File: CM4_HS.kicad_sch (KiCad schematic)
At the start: 7 parts, among them J14 CM4/5 Module B, SW3 SW_Slide_DPDT

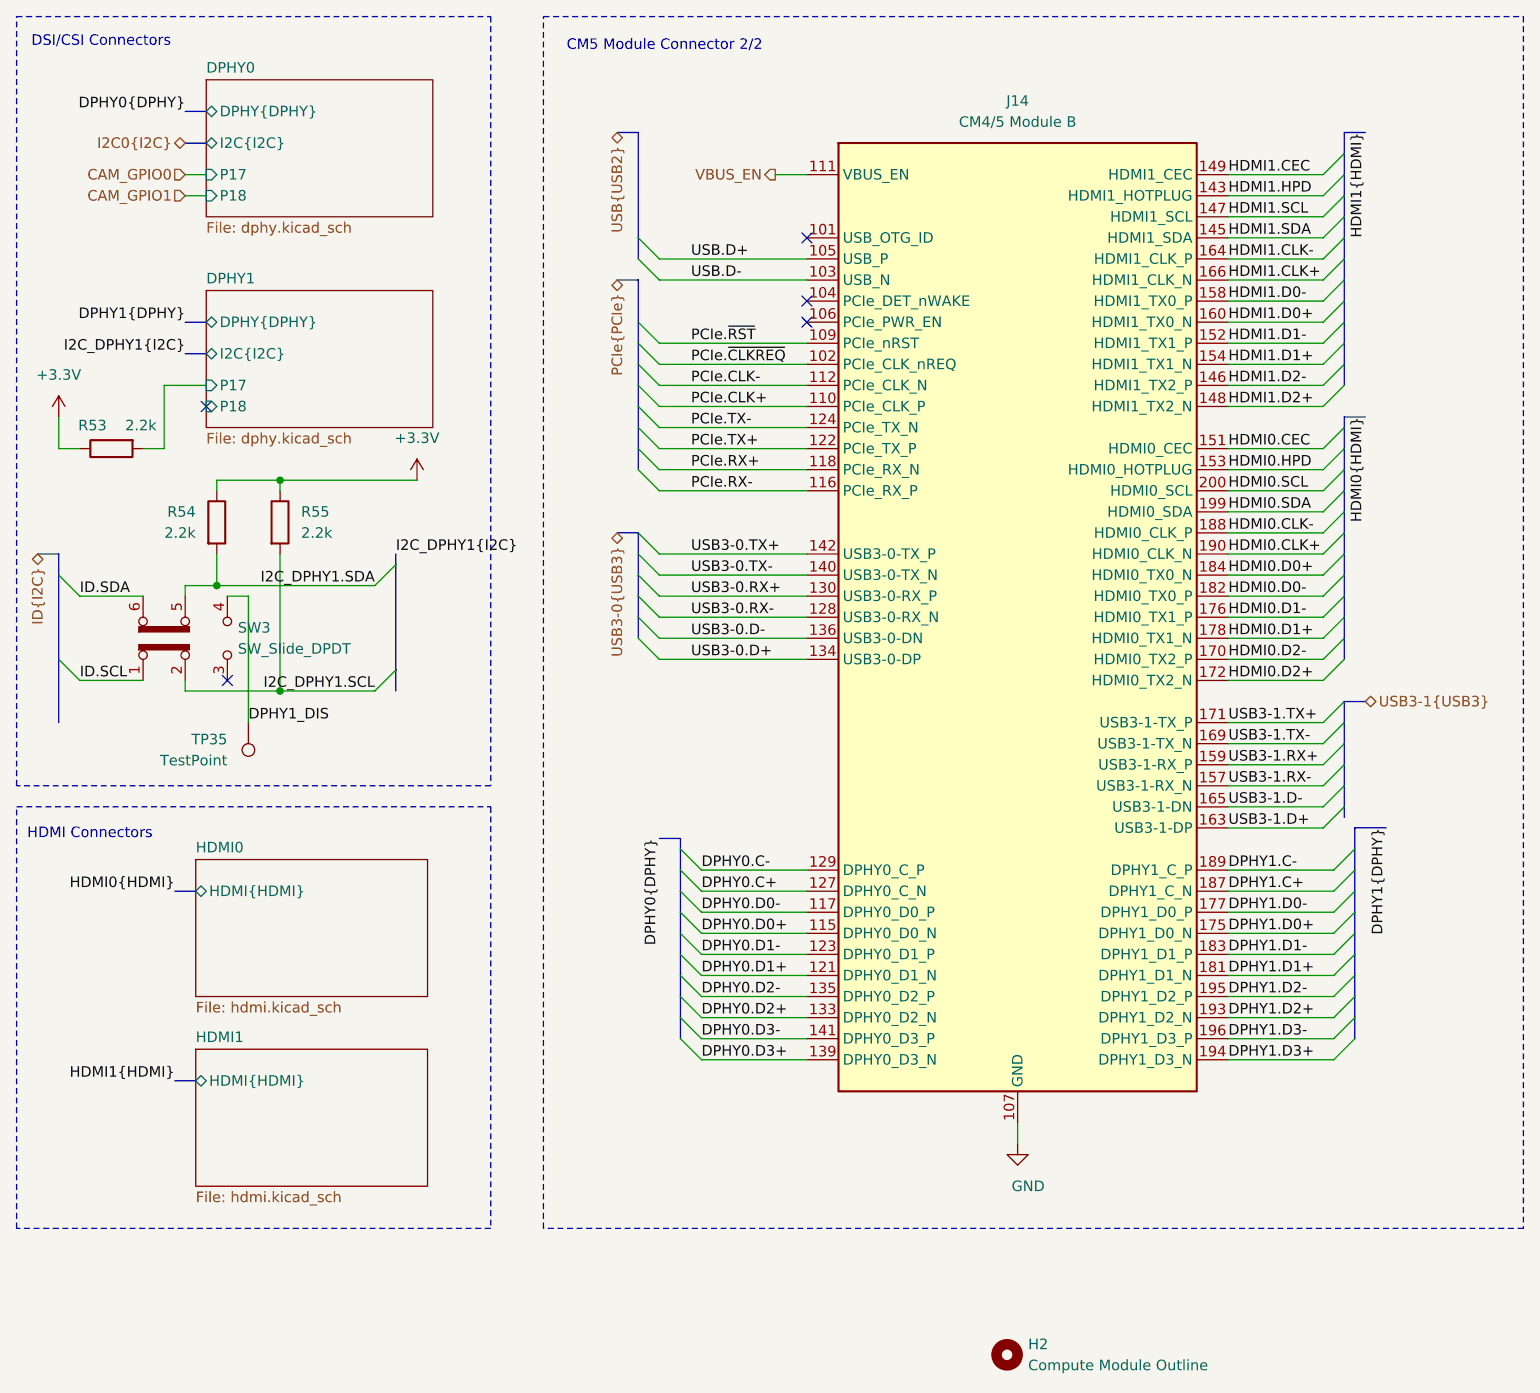
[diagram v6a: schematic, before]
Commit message: Fix HDMI and DSI pinouts, again
Also add the missing LM74800 diode
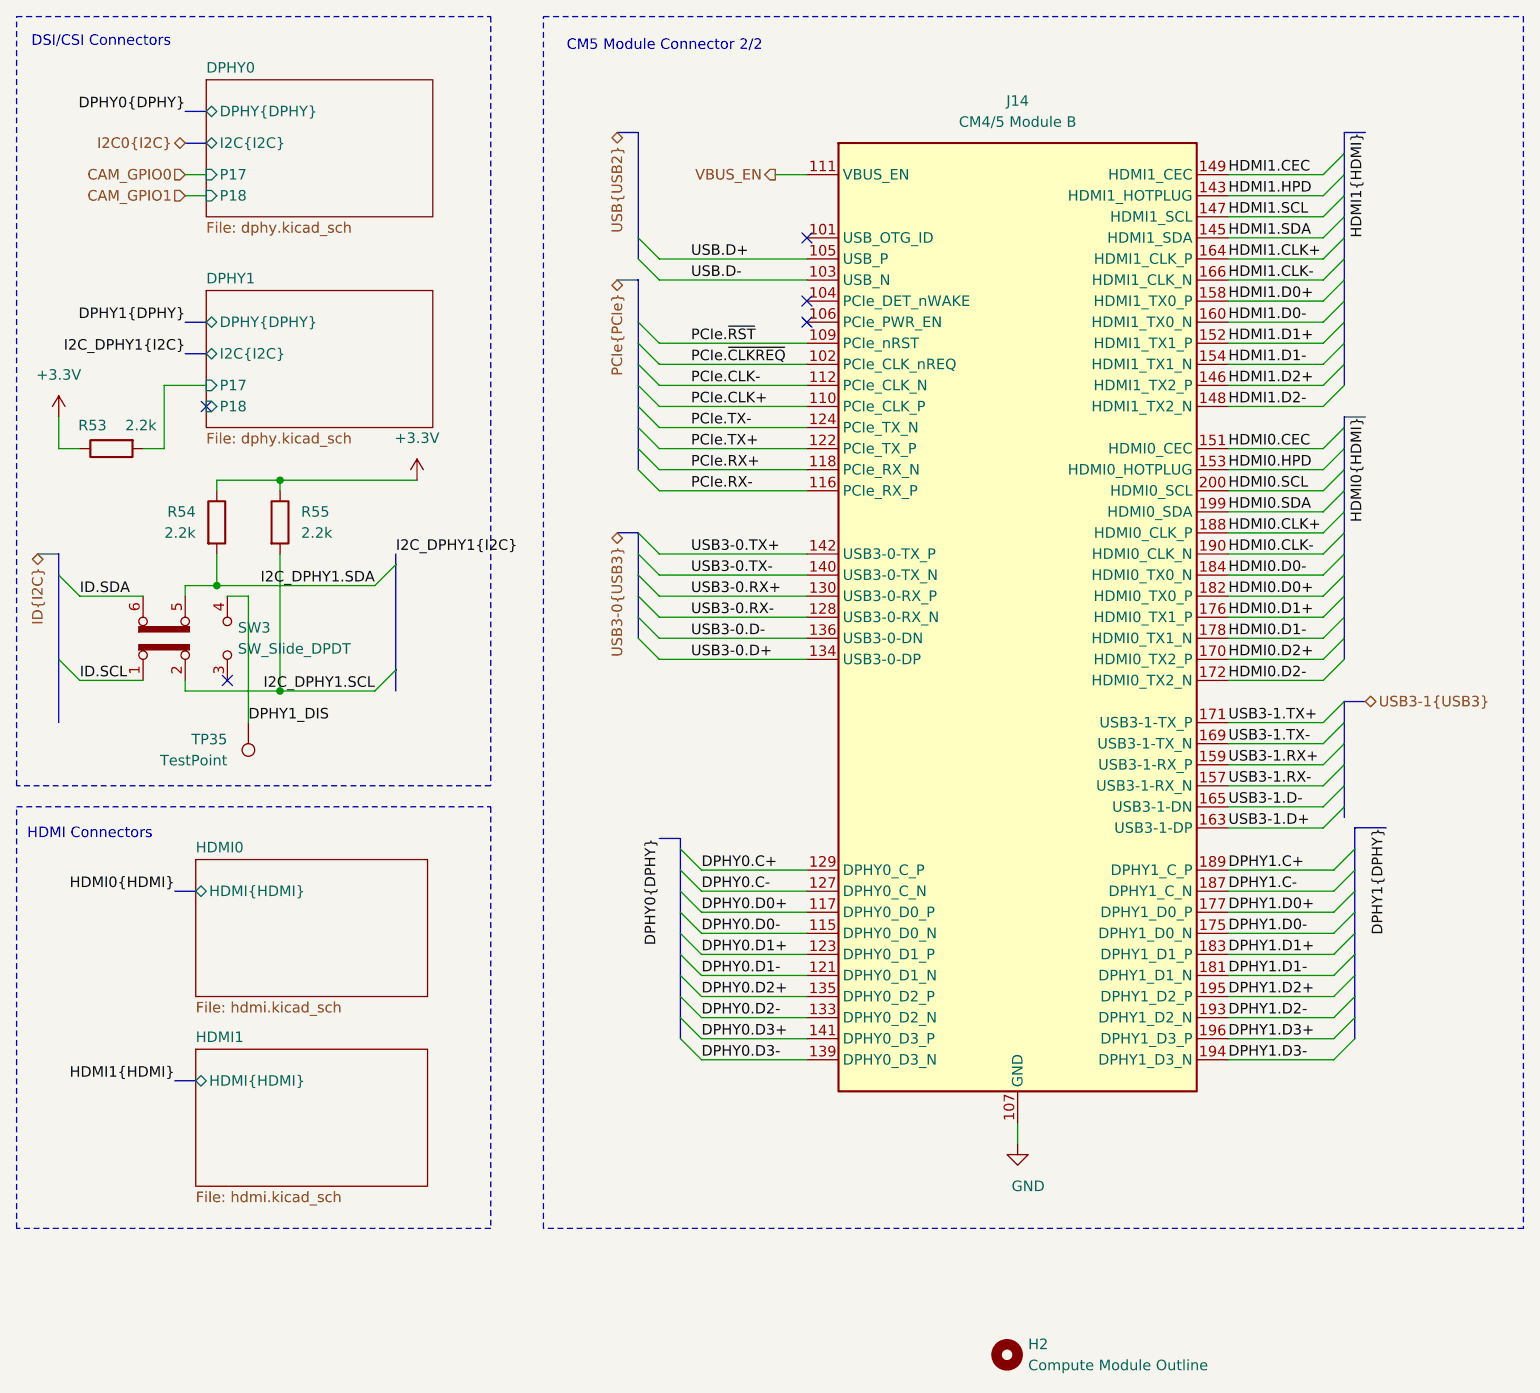
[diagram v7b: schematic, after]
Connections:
- net DPHY0.C+: now also J14.129 (DPHY0_C_P); no longer J14.127 (DPHY0_C_N)
- net DPHY0.C-: now also J14.127 (DPHY0_C_N); no longer J14.129 (DPHY0_C_P)
- net DPHY0.D0+: now also J14.117 (DPHY0_D0_P); no longer J14.115 (DPHY0_D0_N)
- net DPHY0.D0-: now also J14.115 (DPHY0_D0_N); no longer J14.117 (DPHY0_D0_P)
- net DPHY0.D1+: now also J14.123 (DPHY0_D1_P); no longer J14.121 (DPHY0_D1_N)
- net DPHY0.D1-: now also J14.121 (DPHY0_D1_N); no longer J14.123 (DPHY0_D1_P)
- net DPHY0.D2+: now also J14.135 (DPHY0_D2_P); no longer J14.133 (DPHY0_D2_N)
- net DPHY0.D2-: now also J14.133 (DPHY0_D2_N); no longer J14.135 (DPHY0_D2_P)
- net DPHY0.D3+: now also J14.141 (DPHY0_D3_P); no longer J14.139 (DPHY0_D3_N)
- net DPHY0.D3-: now also J14.139 (DPHY0_D3_N); no longer J14.141 (DPHY0_D3_P)
- net DPHY1.C+: now also J14.189 (DPHY1_C_P); no longer J14.187 (DPHY1_C_N)
- net DPHY1.C-: now also J14.187 (DPHY1_C_N); no longer J14.189 (DPHY1_C_P)
- net DPHY1.D0+: now also J14.177 (DPHY1_D0_P); no longer J14.175 (DPHY1_D0_N)
- net DPHY1.D0-: now also J14.175 (DPHY1_D0_N); no longer J14.177 (DPHY1_D0_P)
- net DPHY1.D1+: now also J14.183 (DPHY1_D1_P); no longer J14.181 (DPHY1_D1_N)
- net DPHY1.D1-: now also J14.181 (DPHY1_D1_N); no longer J14.183 (DPHY1_D1_P)
- net DPHY1.D2+: now also J14.195 (DPHY1_D2_P); no longer J14.193 (DPHY1_D2_N)
- net DPHY1.D2-: now also J14.193 (DPHY1_D2_N); no longer J14.195 (DPHY1_D2_P)
- net DPHY1.D3+: now also J14.196 (DPHY1_D3_P); no longer J14.194 (DPHY1_D3_N)
- net DPHY1.D3-: now also J14.194 (DPHY1_D3_N); no longer J14.196 (DPHY1_D3_P)
- net HDMI0.CLK+: now also J14.188 (HDMI0_CLK_P); no longer J14.190 (HDMI0_CLK_N)
- net HDMI0.CLK-: now also J14.190 (HDMI0_CLK_N); no longer J14.188 (HDMI0_CLK_P)
- net HDMI0.D0+: now also J14.182 (HDMI0_TX0_P); no longer J14.184 (HDMI0_TX0_N)
- net HDMI0.D0-: now also J14.184 (HDMI0_TX0_N); no longer J14.182 (HDMI0_TX0_P)
- net HDMI0.D1+: now also J14.176 (HDMI0_TX1_P); no longer J14.178 (HDMI0_TX1_N)
- net HDMI0.D1-: now also J14.178 (HDMI0_TX1_N); no longer J14.176 (HDMI0_TX1_P)
- net HDMI0.D2+: now also J14.170 (HDMI0_TX2_P); no longer J14.172 (HDMI0_TX2_N)
- net HDMI0.D2-: now also J14.172 (HDMI0_TX2_N); no longer J14.170 (HDMI0_TX2_P)
- net HDMI1.CLK+: now also J14.164 (HDMI1_CLK_P); no longer J14.166 (HDMI1_CLK_N)
- net HDMI1.CLK-: now also J14.166 (HDMI1_CLK_N); no longer J14.164 (HDMI1_CLK_P)
- net HDMI1.D0+: now also J14.158 (HDMI1_TX0_P); no longer J14.160 (HDMI1_TX0_N)
- net HDMI1.D0-: now also J14.160 (HDMI1_TX0_N); no longer J14.158 (HDMI1_TX0_P)
- net HDMI1.D1+: now also J14.152 (HDMI1_TX1_P); no longer J14.154 (HDMI1_TX1_N)
- net HDMI1.D1-: now also J14.154 (HDMI1_TX1_N); no longer J14.152 (HDMI1_TX1_P)
- net HDMI1.D2+: now also J14.146 (HDMI1_TX2_P); no longer J14.148 (HDMI1_TX2_N)
- net HDMI1.D2-: now also J14.148 (HDMI1_TX2_N); no longer J14.146 (HDMI1_TX2_P)

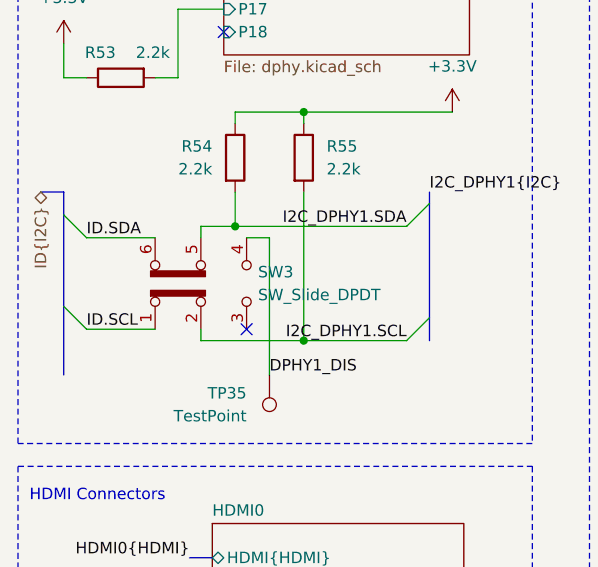
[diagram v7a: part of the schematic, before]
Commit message: Nailed the current limiter design
Also added more GND test pads
Also fixed the MCU I2C pinout
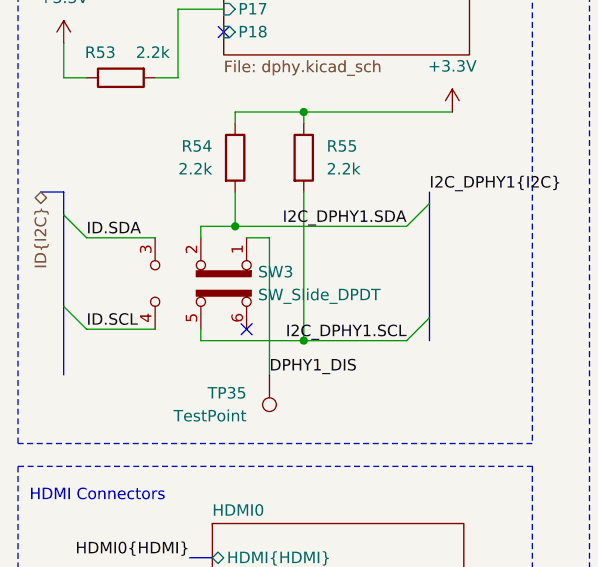
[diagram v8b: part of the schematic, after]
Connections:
- net DPHY1_DIS: now also SW3.1 (A); no longer SW3.4 (A)
- net I2C_DPHY1.SCL: now also SW3.5 (B); no longer SW3.2 (B)
- net I2C_DPHY1.SDA: now also SW3.2 (B); no longer SW3.5 (B)
- net ID.SCL: now also SW3.4 (A); no longer SW3.1 (A)
- net ID.SDA: now also SW3.3 (C); no longer SW3.6 (C)
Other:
- moved on the sheet: SW3
